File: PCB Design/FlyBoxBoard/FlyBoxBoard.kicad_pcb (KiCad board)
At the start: 2 copper layers, 148.6 x 119.4 mm, 45 parts, among them J1 5V in, J10 RED, J11 GREEN, J12 WHITE, J13 INFRARED, J14 LCD Screen, J15 SD card reader, J16 5KΩ, J17 5KΩ, J18 ESP 32 Left Side extra pinouts, J19 ESP 32 Left Side extra pinouts, J2 12V in, J20 Transistor, J21 Logic Level LV pins, J22 Potentiometer, J23 Logic Level Left Side LV, J25 ESP 32 Right Side extra pinou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, J26 BuckPuck IR, J27 Logic Level Right Side HV, J28 Logic Level HV pins, J29 5KΩ, J3 ESP 32 Left Side, J30 5KΩ, J31 5KΩ, J32 5KΩ, J33 5KΩ, J34 5KΩ, J35 Transistor, J36 Transistor, J37 Transistor, J38 BuckPuck White, J39 BuckPuck Green, J4 Real Time Controller, J40 BuckPuck Red, J5 ESP 32 Right Side, J6 Rotary Knob, J9 FANS

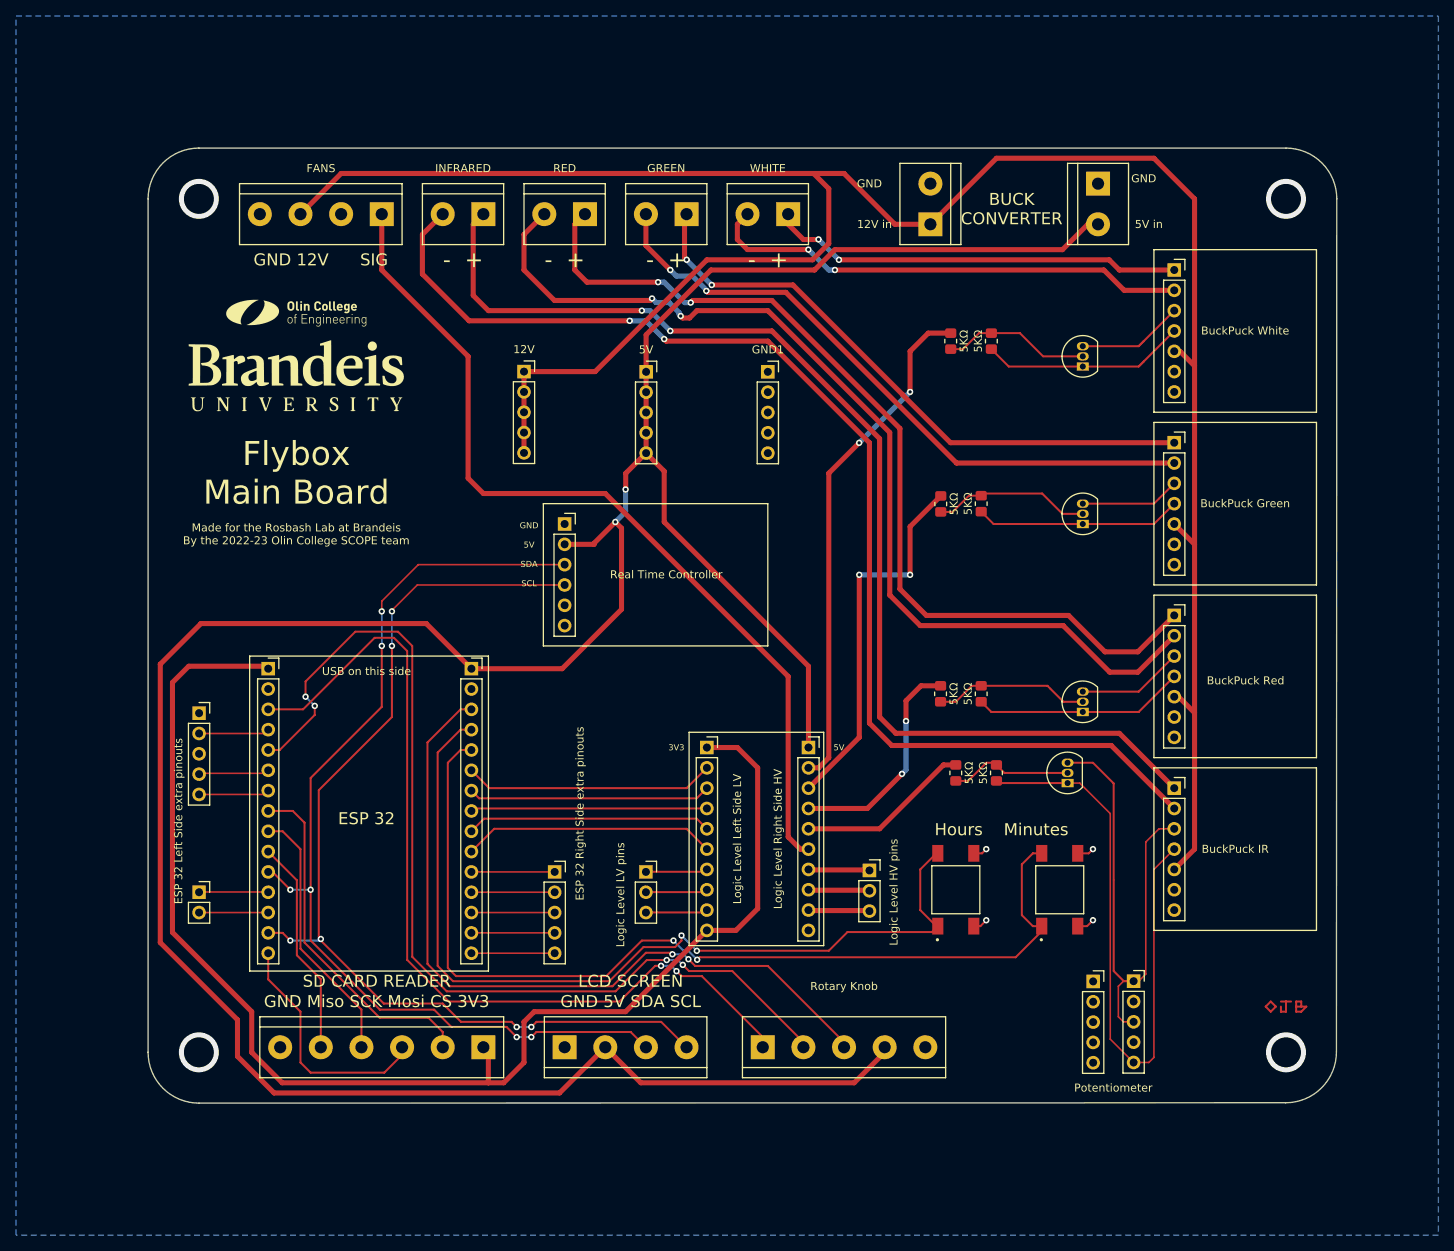
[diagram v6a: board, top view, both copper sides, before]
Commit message: Shrunk vias, fixed ohms and XV1 labels
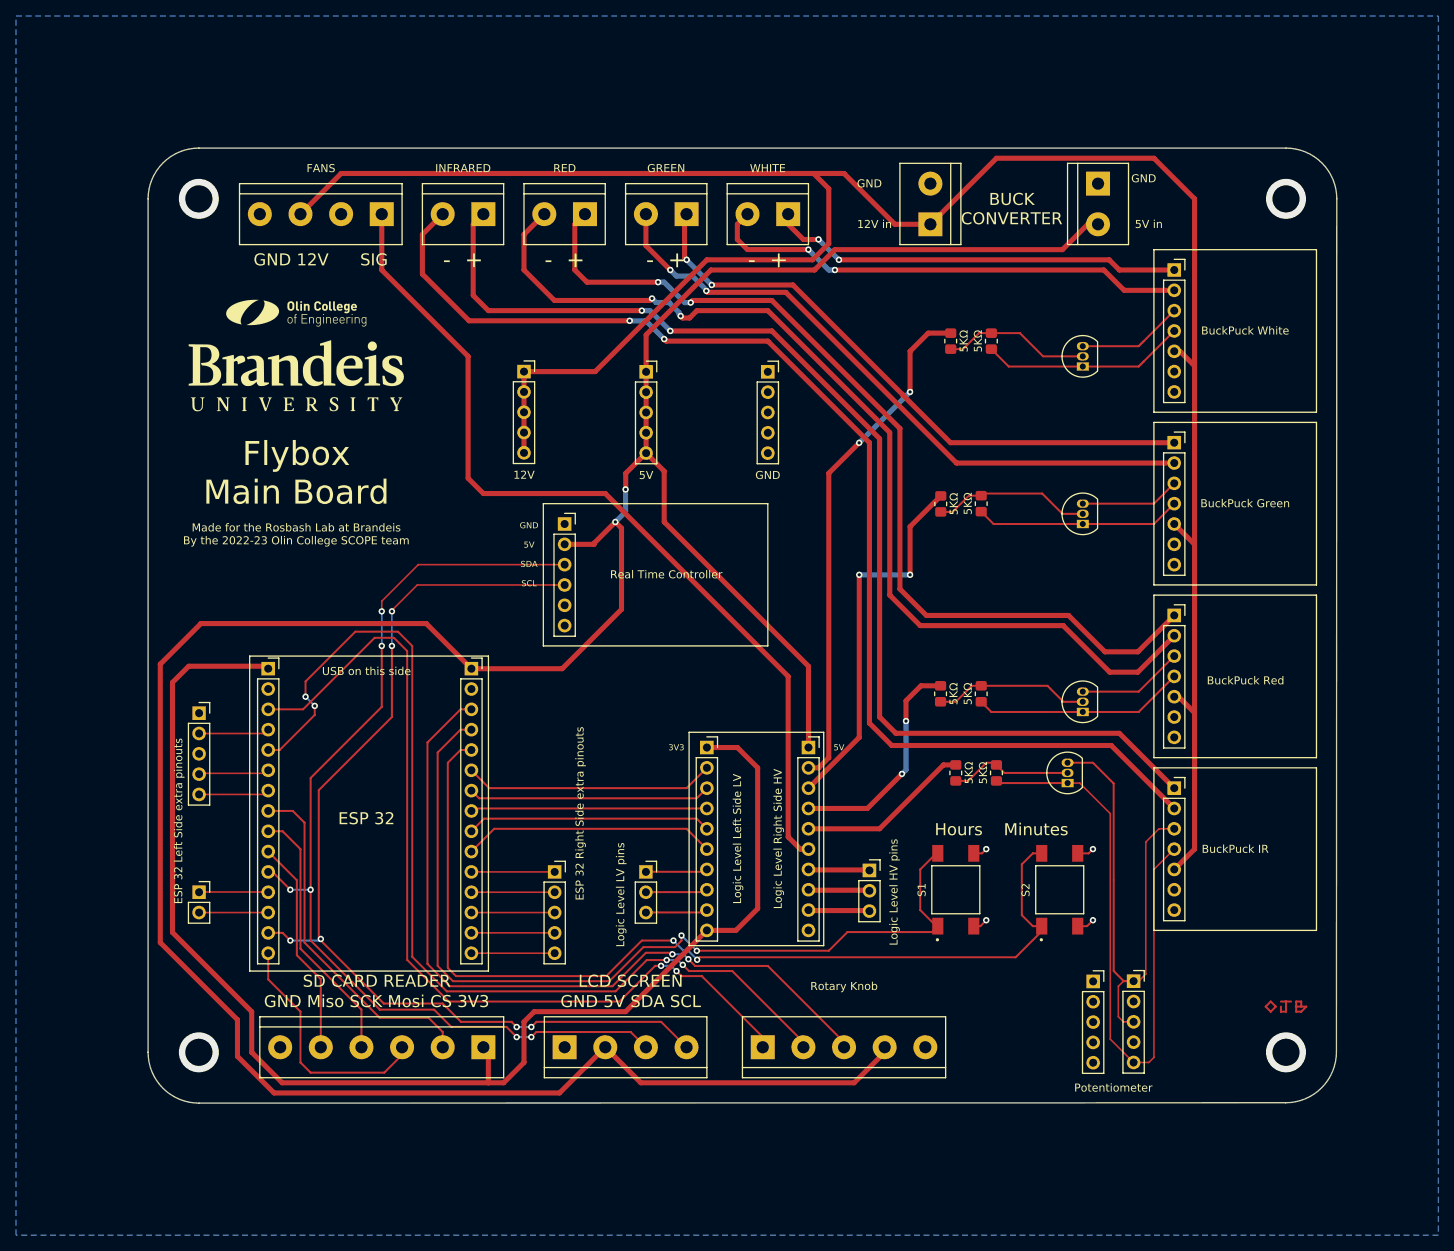
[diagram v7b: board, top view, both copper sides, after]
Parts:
- J24: renamed from GND1; value Extra pinouts GND -> GND
- J7: renamed from 5V; value Extra pinouts 5V -> 5V
- J8: renamed from 12V; value Extra pinouts 12V -> 12V
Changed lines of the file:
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@@
     (property "Sheetname" "")
     (attr through_hole)
-    (fp_text reference "GND1" (at 0 -2.77) (layer "F.SilkS")
-      (effects (font (size 1 1) (thickness 0.15)))
-    )
-    (fp_text value "Extra pinouts GND" (at 1.88 12.93) (layer "F.Fab")
+    (fp_text reference "J24" (at 0 -2.77) (layer "F.Fab")
+      (effects (font (size 1 1) (thickness 0.15)))
+    )
+    (fp_text value "GND" (at 0 12.93) (layer "F.SilkS")
       (effects (font (size 1 1) (thickness 0.15)))
     )
@@
     (property "Sheetname" "")
     (attr through_hole)
-    (fp_text reference "5V" (at 0 -2.77) (layer "F.SilkS")
-      (effects (font (size 1 1) (thickness 0.15)))
-    )
-    (fp_text value "Extra pinouts 5V" (at 0 12.93) (layer "F.Fab")
+    (fp_text reference "J7" (at 0 -2.77) (layer "F.Fab")
+      (effects (font (size 1 1) (thickness 0.15)))
+    )
+    (fp_text value "5V" (at 0 12.93) (layer "F.SilkS")
       (effects (font (size 1 1) (thickness 0.15)))
     )
@@
     (property "Sheetname" "")
     (attr smd)
-    (fp_text reference "S2" (at -0.025 -4.235 90) (layer "F.Fab")
+    (fp_text reference "S2" (at -0.025 -4.235 90) (layer "F.SilkS")
       (effects (font (size 1 1) (thickness 0.15)))
     )
@@
     (fp_line (start 3 -3) (end 3 3) (layer "F.SilkS") (width 0.127))
     (fp_line (start 3 -3) (end -3 -3) (layer "F.SilkS") (width 0.127))
+    (fp_line (start 3 3) (end -3 3) (layer "F.SilkS") (width 0.127))
     (fp_line (start -3 3) (end -3 -3) (layer "F.SilkS") (width 0.127))
-    (fp_line (start 3 3) (end -3 3) (layer "F.SilkS") (width 0.127))
     (fp_circle (center -6.25 -2.3) (end -6.15 -2.3) (layer "F.SilkS") (width 0.2) (fill none))
     (fp_line (start -5.85 -3.25) (end -5.85 3.25) (layer "F.CrtYd") (width 0.05))
-    (fp_line (start 5.85 -3.25) (end -5.85 -3.25) (layer "F.CrtYd") (width 0.05))
     (fp_line (start -5.85 3.25) (end 5.85 3.25) (layer "F.CrtYd") (width 0.05))
     (fp_line (start 5.85 3.25) (end 5.85 -3.25) (layer "F.CrtYd") (width 0.05))
+    (fp_line (start 5.85 -3.25) (end -5.85 -3.25) (layer "F.CrtYd") (width 0.05))
+    (fp_line (start -3 3) (end 3 3) (layer "F.Fab") (width 0.127))
+    (fp_line (start 3 -3) (end -3 -3) (layer "F.Fab") (width 0.127))
     (fp_line (start -3 -3) (end -3 3) (layer "F.Fab") (width 0.127))
-    (fp_line (start -3 3) (end 3 3) (layer "F.Fab") (width 0.127))
     (fp_line (start 3 3) (end 3 -3) (layer "F.Fab") (width 0.127))
-    (fp_line (start 3 -3) (end -3 -3) (layer "F.Fab") (width 0.127))
     (fp_circle (center -6.25 -2.3) (end -6.15 -2.3) (layer "F.Fab") (width 0.2) (fill none))
     (pad "1" smd rect locked (at -4.55 -2.25 90) (size 2.1 1.4) (layers "F.Cu" "F.Paste" "F.Mask")
@@
     (property "Sheetname" "")
     (attr through_hole)
-    (fp_text reference "12V" (at 0 -2.77) (layer "F.SilkS")
-      (effects (font (size 1 1) (thickness 0.15)))
-    )
-    (fp_text value "Extra pinouts 12V" (at 0 12.93) (layer "F.Fab")
+    (fp_text reference "J8" (at 0 -2.77) (layer "F.Fab")
+      (effects (font (size 1 1) (thickness 0.15)))
+    )
+    (fp_text value "12V" (at 0 12.93) (layer "F.SilkS")
       (effects (font (size 1 1) (thickness 0.15)))
     )
@@
     (property "Sheetname" "")
     (attr smd)
-    (fp_text reference "S1" (at -0.025 -4.235 90) (layer "F.Fab")
+    (fp_text reference "S1" (at -0.025 -4.235 90) (layer "F.SilkS")
       (effects (font (size 1 1) (thickness 0.15)))
     )
@@
     )
     (fp_line (start 3 -3) (end 3 3) (layer "F.SilkS") (width 0.127))
+    (fp_line (start 3 -3) (end -3 -3) (layer "F.SilkS") (width 0.127))
     (fp_line (start 3 3) (end -3 3) (layer "F.SilkS") (width 0.127))
-    (fp_line (start 3 -3) (end -3 -3) (layer "F.SilkS") (width 0.127))
     (fp_line (start -3 3) (end -3 -3) (layer "F.SilkS") (width 0.127))
     (fp_circle (center -6.25 -2.3) (end -6.15 -2.3) (layer "F.SilkS") (width 0.2) (fill none))
     (fp_line (start 5.85 3.25) (end 5.85 -3.25) (layer "F.CrtYd") (width 0.05))
+    (fp_line (start -5.85 -3.25) (end -5.85 3.25) (layer "F.CrtYd") (width 0.05))
     (fp_line (start -5.85 3.25) (end 5.85 3.25) (layer "F.CrtYd") (width 0.05))
     (fp_line (start 5.85 -3.25) (end -5.85 -3.25) (layer "F.CrtYd") (width 0.05))
-    (fp_line (start -5.85 -3.25) (end -5.85 3.25) (layer "F.CrtYd") (width 0.05))
+    (fp_line (start -3 3) (end 3 3) (layer "F.Fab") (width 0.127))
     (fp_line (start 3 3) (end 3 -3) (layer "F.Fab") (width 0.127))
+    (fp_line (start 3 -3) (end -3 -3) (layer "F.Fab") (width 0.127))
     (fp_line (start -3 -3) (end -3 3) (layer "F.Fab") (width 0.127))
-    (fp_line (start 3 -3) (end -3 -3) (layer "F.Fab") (width 0.127))
-    (fp_line (start -3 3) (end 3 3) (layer "F.Fab") (width 0.127))
     (fp_circle (center -6.25 -2.3) (end -6.15 -2.3) (layer "F.Fab") (width 0.2) (fill none))
     (pad "1" smd rect locked (at -4.55 -2.25 90) (size 2.1 1.4) (layers "F.Cu" "F.Paste" "F.Mask")
@@
     (pts (xy 31.5268 81.5882) (xy 56.9268 81.5882))
     (height -5.08)
-    (gr_text "1.0000 in" (at 44.2268 74.7082) (layer "F.Fab")
+    (gr_text "25.4000 mm" (at 44.2268 74.7082) (layer "F.Fab")
       (effects (font (size 1.5 1.5) (thickness 0.3)))
     )
@@
     (pts (xy 86.36 91.44) (xy 99.06 91.44))
     (height -6.35)
-    (gr_text "0.5000 in" (at 92.71 83.94) (layer "F.Fab")
+    (gr_text "12.7000 mm" (at 92.71 83.94) (layer "F.Fab")
       (effects (font (size 1 1) (thickness 0.15)))
     )
@@
   (segment (start 134.62 113.03) (end 133.88 113.77) (width 0.25) (layer "F.Cu") (net 1))
   (segment (start 133.88 113.77) (end 132.715 113.77) (width 0.25) (layer "F.Cu") (net 1))
-  (via (at 22.86 129.54) (size 5) (drill 3.75) (layers "F.Cu" "B.Cu") (free) (net 1))
+  (via (at 22.86 129.54) (size 5) (drill 3.4) (layers "F.Cu" "B.Cu") (free) (net 1))
   (via (at 134.62 104.14) (size 0.8) (drill 0.4) (layers "F.Cu" "B.Cu") (net 1))
   (via (at 134.62 113.03) (size 0.8) (drill 0.4) (layers "F.Cu" "B.Cu") (net 1))
   (via (at 121.285 113.03) (size 0.8) (drill 0.4) (layers "F.Cu" "B.Cu") (net 1))
   (via (at 121.285 104.14) (size 0.8) (drill 0.4) (layers "F.Cu" "B.Cu") (net 1))
-  (via (at 158.75 22.86) (size 5) (drill 3.75) (layers "F.Cu" "B.Cu") (free) (net 1))
-  (via (at 158.75 129.54) (size 5) (drill 3.75) (layers "F.Cu" "B.Cu") (free) (net 1))
-  (via (at 22.86 22.86) (size 5) (drill 3.75) (layers "F.Cu" "B.Cu") (free) (net 1))
+  (via (at 158.75 22.86) (size 5) (drill 3.4) (layers "F.Cu" "B.Cu") (free) (net 1))
+  (via (at 158.75 129.54) (size 5) (drill 3.4) (layers "F.Cu" "B.Cu") (free) (net 1))
+  (via (at 22.86 22.86) (size 5) (drill 3.4) (layers "F.Cu" "B.Cu") (free) (net 1))
   (segment (start 102.362 29.21) (end 130.81 29.21) (width 0.635) (layer "F.Cu") (net 2))
   (segment (start 108.585 128.905) (end 108.585 129.54) (width 0.635) (layer "F.Cu") (net 2))

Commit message: Zachary second pass on FlyBoxBoard
Pretty much ready to go after OJ checks again and reviews my notes in Teams.

I still have not checked the other two boards.
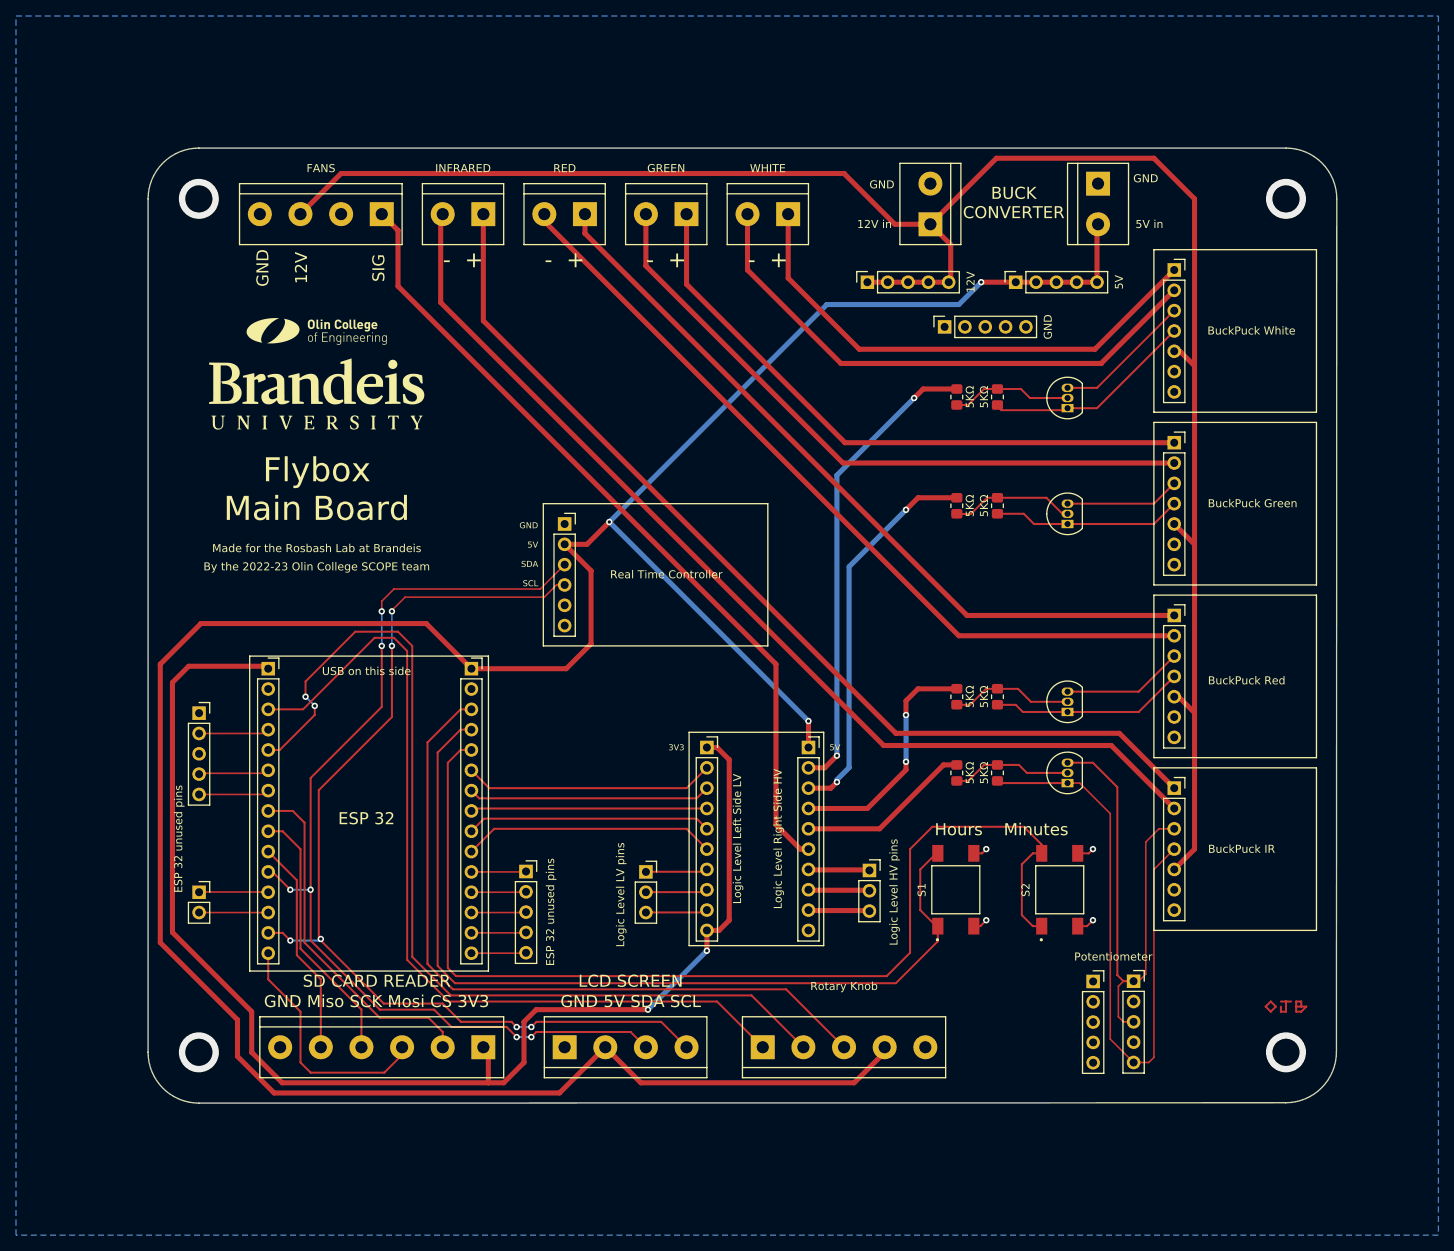
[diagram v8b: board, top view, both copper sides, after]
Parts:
- J18: value ESP 32 Left Side extra pinouts -> ESP 32 unused pins
- J25: value ESP 32 Right Side extra pinouts -> ESP 32 unused pins
- moved J7 47.5 mm to (125.0, 33.3), turned to 90 degrees
- moved J8 44.4 mm to (106.4, 33.3), turned to 90 degrees
- moved J24 22.8 mm to (116.1, 38.9), turned to 90 degrees
- moved J29 7.03 mm to (122.7, 47.6)
- moved J30 7.03 mm to (117.6, 47.6)
- moved J35 5.54 mm to (131.4, 49.0)
- moved J25 3.58 mm to (63.8, 106.9)
- moved G*** 3.43 mm to (37.6, 47.4)
- moved G*** 3.43 mm to (37.4, 39.4)
- moved J34 2.06 mm to (117.6, 85.1)
- moved J33 2.06 mm to (122.7, 85.1)
- moved J31 2.05 mm to (122.7, 61.2)
- moved J32 2.02 mm to (117.6, 61.2)
- moved J36 1.91 mm to (131.4, 63.5)
- moved J37 1.91 mm to (131.4, 87.0)
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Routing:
- net /12V: track 281.6 -> 235.7 mm
- net /R LED-: track 125.0 -> 101.1 mm, vias 2 -> 0
- net /IR LED-: track 150.7 -> 129.0 mm, vias 2 -> 0
- net /IR LED+: track 144.2 -> 123.9 mm, vias 2 -> 0
- net /R LED+: track 116.1 -> 95.9 mm, vias 2 -> 0
- net /5V: track 358.6 -> 341.5 mm, vias 2 -> 3
- net /D14: track 121.3 -> 133.7 mm, vias 2 -> 0
- net /W LED+: track 51.9 -> 64.0 mm, vias 2 -> 0
- net /HV5: track 111.0 -> 102.1 mm
- net /W LED-: track 60.9 -> 69.0 mm, vias 2 -> 0
- net /HV1: track 64.1 -> 58.7 mm
- net /D15: track 113.8 -> 109.3 mm, vias 2 -> 0
- net Net-(J31-Pad1): track 19.8 -> 15.5 mm
- net /3V3: track 169.8 -> 165.6 mm, vias 0 -> 2
- net /D13: track 95.1 -> 91.3 mm, vias 2 -> 0
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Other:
- board text added: "By the 2022-23 Olin College SCOPE team"
- board text added: "Made for the Rosbash Lab at Brandeis"
- board text removed: "Made for the Rosbash Lab at Brandeis By the 2022-23 Olin College SCOPE team"
